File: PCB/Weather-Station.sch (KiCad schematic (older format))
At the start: 49 parts, among them J1 Biruta, J10 Conn_01x02, J11 Conn_01x02, J12 Conn_01x02, J13 Conn_01x02, J14 Conn_01x02, J15 Conn_01x02, J2 Power, J3 DataLogger, J4 BME280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

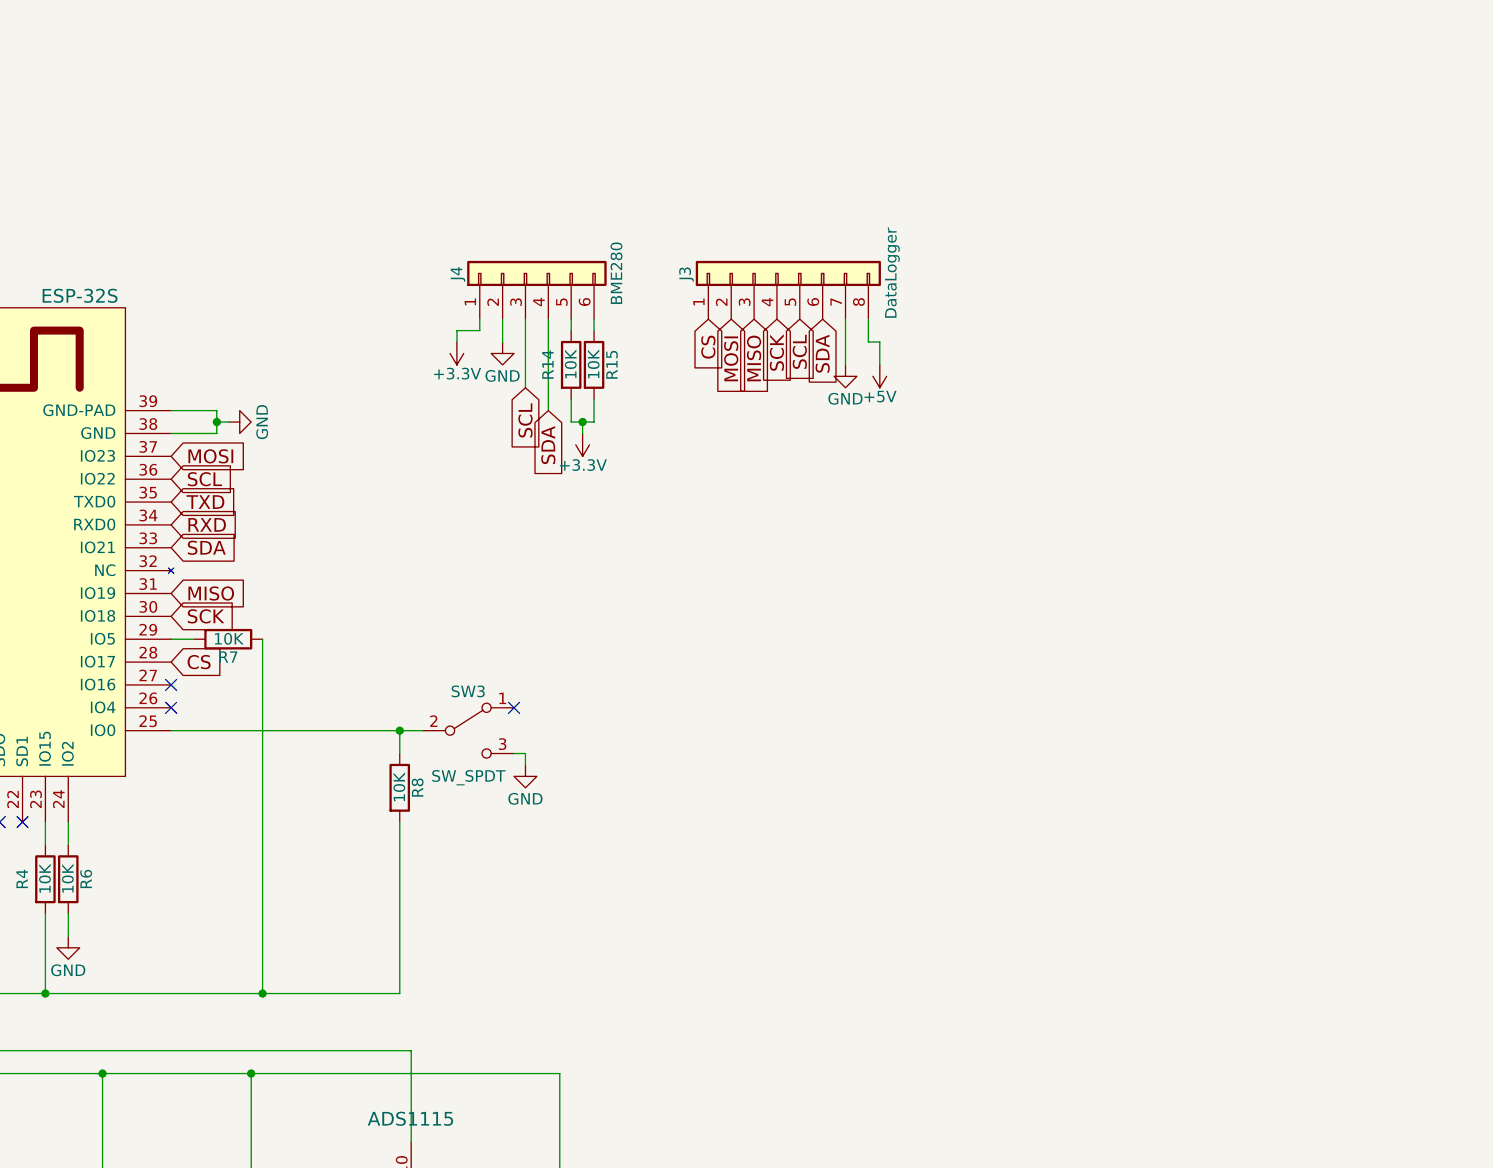
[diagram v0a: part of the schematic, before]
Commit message: Adicionando componentes do data logger
Signed-off-by: Gustavo Costa <gustavocosta@ic.ufal.br>
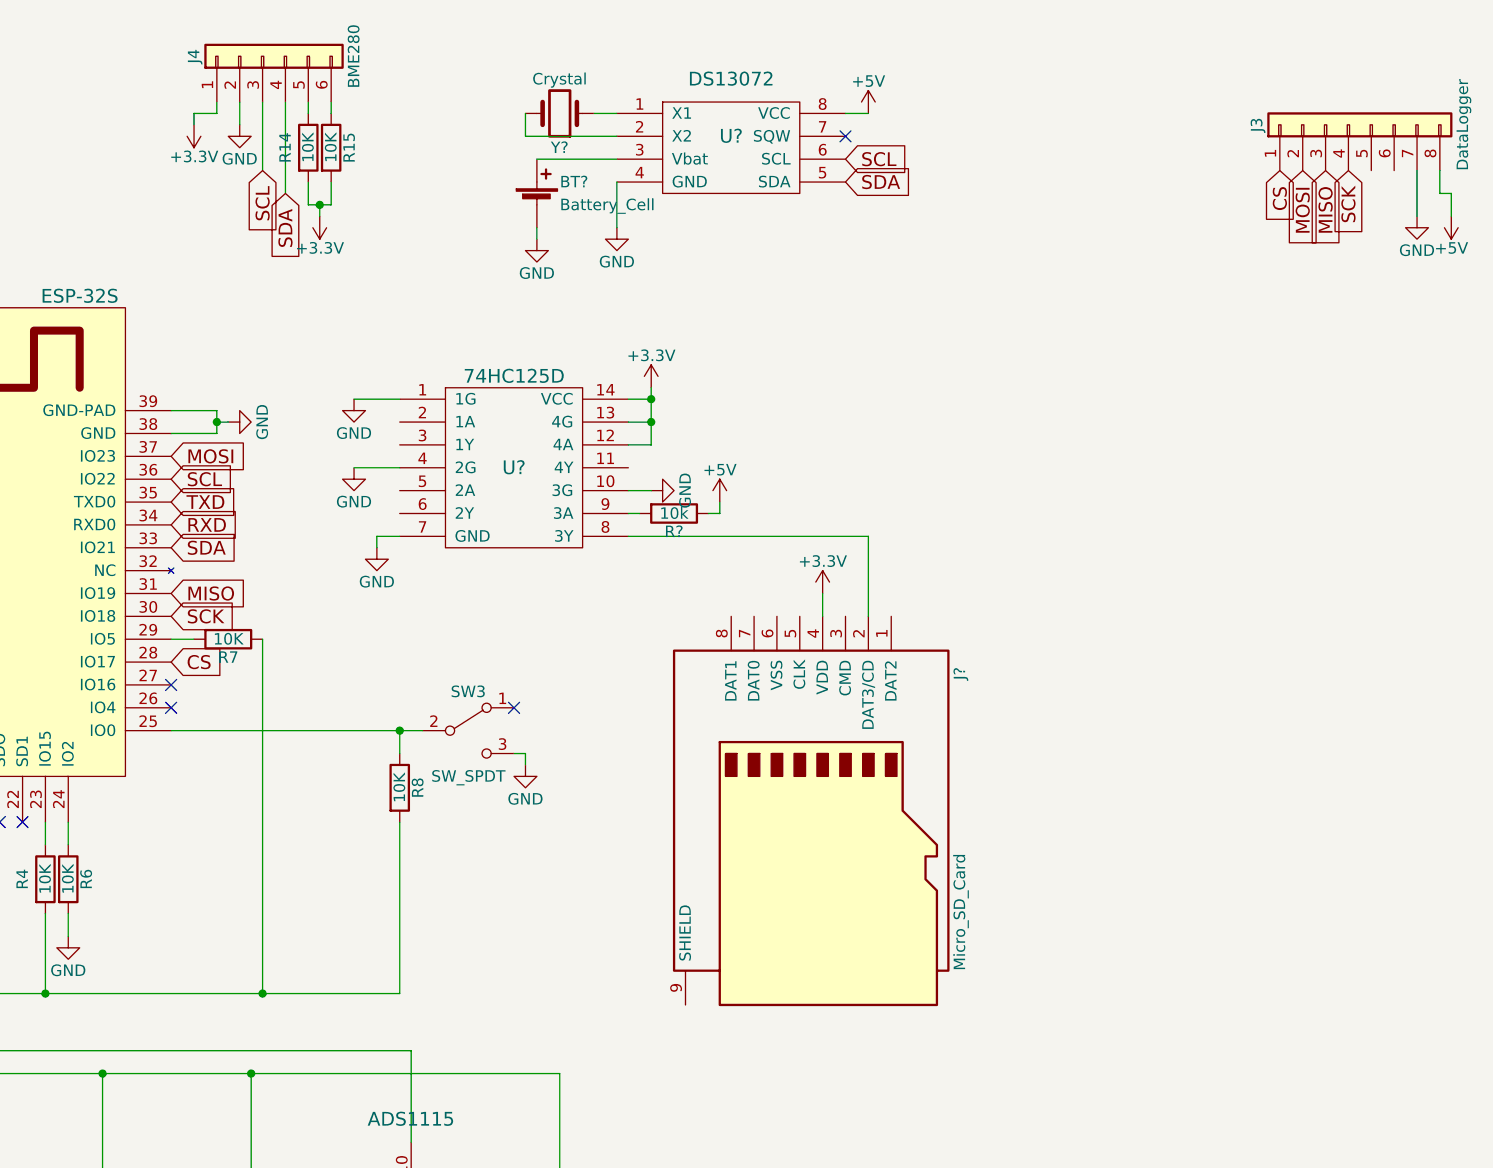
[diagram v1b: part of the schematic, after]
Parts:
- added BT?: Battery_Cell, symbol Battery_Cell
- added J?: Micro_SD_Card, symbol Micro_SD_Card
- added R?: 10k, symbol R
- added U?: DS13072, symbol DS13072
- added U?: 74HC125D, symbol 74HC125D
- added Y?: Crystal, symbol Crystal
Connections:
- net +3V3: now also J?.4 (VDD), U?.12 (4A), U?.13 (4G), U?.14 (VCC)
- net +5V: now also R?.1, U?.8 (VCC)
- net GND: now also BT?.2 (-), U?.1 (1G), U?.10 (3G), U?.4 (2G), U?.4 (GND), U?.7 (GND)
- net SCL: now also U?.6 (SCL); no longer J3.5 (Pin_5)
- net SDA: now also U?.5 (SDA); no longer J3.6 (Pin_6)
- new net: U?.1 (X1), Y?.1
- new net: U?.2 (X2), Y?.2
- new net: BT?.1 (+), U?.3 (Vbat)
- new net: J?.2 (DAT3/CD), U?.8 (3Y)
- new net: R?.2, U?.9 (3A)
- no-connect marks 20 -> 21
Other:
- moved on the sheet: J3, J4, R14, R15

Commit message: Fazendo PCB com o data logger
Signed-off-by: Gustavo Costa <gustavocosta@ic.ufal.br>
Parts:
- removed J3: DataLogger, Pin_Headers:Pin_Header_Straight_1x08_Pitch2.54mm, symbol Conn_01x08
- removed U?: 74HC125D, symbol 74HC125D
- added U8: 74HC125D, Housings_SOIC:SOIC-14_3.9x8.7mm_Pitch1.27mm, symbol 74HC125D
- BT1: renamed from BT?; footprint (none) -> Battery_Holders:Keystone_3000_1x12mm-CoinCell
- J3: renamed from J?; footprint (none) -> MPPT_Library:Conn_uSDcard
- R12: renamed from R?; footprint (none) -> Resistors_SMD:R_0805
- U9: renamed from U?; footprint (none) -> Housings_SOIC:SOIC-8_3.9x4.9mm_Pitch1.27mm
- Y1: renamed from Y?; footprint (none) -> Crystals:Crystal_DS15_d1.5mm_l5.0mm_Horizontal
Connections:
- net +3V3: now also J4.6 (Pin_6), U8.12 (4A), U8.13 (4G), U8.14 (VCC); no longer J4.1 (Pin_1)
- net CS: now also R12.2, U8.9 (3A)
- net GND: now also J3.6 (VSS), J3.9 (SHIELD), J4.5 (Pin_5), U8.1 (1G), U8.10 (3G), U8.4 (2G), U8.7 (GND); no longer J4.2 (Pin_2)
- net MISO: now also J3.7 (DAT0)
- net MOSI: now also U8.5 (2A)
- net SCK: now also U8.2 (1A)
- net SCL: now also J4.4 (Pin_4); no longer J4.3 (Pin_3)
- net SDA: now also J4.3 (Pin_3); no longer J4.4 (Pin_4)
- net at R14.1: now also J4.2 (Pin_2); no longer J4.5 (Pin_5)
- net at R15.1: now also J4.1 (Pin_1); no longer J4.6 (Pin_6)
- net at J3.2 (DAT3/CD): now also U8.8 (3Y)
- net at J3.3 (CMD): now also U8.6 (2Y)
- net at J3.5 (CLK): now also U8.3 (1Y)
- no-connect marks 21 -> 24
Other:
- moved on the sheet: J3, R12
